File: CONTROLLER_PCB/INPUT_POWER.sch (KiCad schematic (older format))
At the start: 47 parts

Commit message: LED PCB: Changed to 2 layer, added vias and copper (not complete). Controller: Split up ESP32 and input & power sheets in schematic.
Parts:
- added C?: C_Small, symbol C_Small
- added R? (x2): R_Small, symbol R_Small
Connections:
- net GND: now also C?.2, R?.2
- net VIN: now reaches C?.1, C?.1, C?.1, C?.1, C?.1, L?.1, L?.2, R?.1, TP?.1, U?.3 (IN), U?.3 (VIN)
- net at C?.1, C?.1, D?.2 (K)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: now also R?.1
- new net ADC_Vout: C?.1, R?.1, R?.2
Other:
- moved on the sheet: R?, U?A
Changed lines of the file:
@@
 L TS462CDT U?
 U 1 1 5C5A4CCB
-P 6050 6550
-F 0 "U?" H 6050 6750 50  0000 L CNN
-F 1 "TS462CDT" H 6050 6350 50  0000 L CNN
-F 2 "" H 6050 6550 50  0001 C CNN
-F 3 "" H 6050 6550 50  0001 C CNN
-	1    6050 6550
+P 2300 4800
+F 0 "U?" H 2300 5000 50  0000 L CNN
+F 1 "TS462CDT" H 2300 4600 50  0000 L CNN
+F 2 "" H 2300 4800 50  0001 C CNN
+F 3 "" H 2300 4800 50  0001 C CNN
+	1    2300 4800
 	1    0    0    -1
 $EndComp
@@
 L R_Small R?
 U 1 1 5C5A4DE0
-P 10450 1100
-F 0 "R?" V 10650 1050 50  0000 L CNN
-F 1 "R_Small" V 10550 950 50  0000 L CNN
-F 2 "" H 10450 1100 50  0001 C CNN
-F 3 "" H 10450 1100 50  0001 C CNN
-	1    10450 1100
+P 10500 1100
+F 0 "R?" V 10700 1050 50  0000 L CNN
+F 1 "R_Small" V 10600 950 50  0000 L CNN
+F 2 "" H 10500 1100 50  0001 C CNN
+F 3 "" H 10500 1100 50  0001 C CNN
+	1    10500 1100
 	0    -1   -1   0
 $EndComp
@@
 Connection ~ 8200 1700
 Wire Wire Line
-	8950 1100 10350 1100
+	8950 1100 10400 1100
 Wire Wire Line
 	9300 1200 9300 1100
@@
 Wire Wire Line
 	6800 5300 6800 3500
-Wire Wire Line
-	6800 3500 9450 3500
-Wire Wire Line
-	9450 3500 9450 2000
-Wire Wire Line
-	9450 2000 8050 2000
 Wire Wire Line
 	7050 5200 7050 5300
@@
 L GND #PWR?
 U 1 1 5C5A6FF8
-P 5950 7000
-F 0 "#PWR?" H 5950 6750 50  0001 C CNN
-F 1 "GND" H 5950 6850 50  0000 C CNN
-F 2 "" H 5950 7000 50  0001 C CNN
-F 3 "" H 5950 7000 50  0001 C CNN
-	1    5950 7000
+P 2200 5250
+F 0 "#PWR?" H 2200 5000 50  0001 C CNN
+F 1 "GND" H 2200 5100 50  0000 C CNN
+F 2 "" H 2200 5250 50  0001 C CNN
+F 3 "" H 2200 5250 50  0001 C CNN
+	1    2200 5250
 	1    0    0    -1
 $EndComp
@@
 L GND #PWR?
 U 1 1 5C5A7058
-P 5250 6800
-F 0 "#PWR?" H 5250 6550 50  0001 C CNN
-F 1 "GND" H 5250 6650 50  0000 C CNN
-F 2 "" H 5250 6800 50  0001 C CNN
-F 3 "" H 5250 6800 50  0001 C CNN
-	1    5250 6800
-	1    0    0    -1
-$EndComp
-Wire Wire Line
-	6350 6550 6600 6550
-Wire Wire Line
-	6600 6550 6600 7300
-Wire Wire Line
-	6600 7300 5550 7300
-Wire Wire Line
-	5550 7300 5550 6650
-Wire Wire Line
-	5550 6650 5750 6650
-Wire Wire Line
-	5750 6450 5250 6450
-Wire Wire Line
-	5250 6450 5250 6800
-Wire Wire Line
-	5950 6850 5950 7000
+P 1500 5050
+F 0 "#PWR?" H 1500 4800 50  0001 C CNN
+F 1 "GND" H 1500 4900 50  0000 C CNN
+F 2 "" H 1500 5050 50  0001 C CNN
+F 3 "" H 1500 5050 50  0001 C CNN
+	1    1500 5050
+	1    0    0    -1
+$EndComp
+Wire Wire Line
+	2600 4800 2850 4800
+Wire Wire Line
+	2850 4800 2850 5550
+Wire Wire Line
+	2850 5550 1800 5550
+Wire Wire Line
+	1800 5550 1800 4900
+Wire Wire Line
+	1800 4900 2000 4900
+Wire Wire Line
+	2000 4700 1500 4700
+Wire Wire Line
+	1500 4700 1500 5050
+Wire Wire Line
+	2200 5100 2200 5250
 $Comp
 L TEST TP?
@@
 Wire Wire Line
 	5900 3950 5900 3900
+$Comp
+L R_Small R?
+U 1 1 5C58FF67
+P 10300 2000
+F 0 "R?" H 10330 2020 50  0000 L CNN
+F 1 "R_Small" H 10330 1960 50  0000 L CNN
+F 2 "" H 10300 2000 50  0001 C CNN
+F 3 "" H 10300 2000 50  0001 C CNN
+	1    10300 2000
+	1    0    0    -1
+$EndComp
+$Comp
+L GND #PWR?
+U 1 1 5C58FF6D
+P 10300 2250
+F 0 "#PWR?" H 10300 2000 50  0001 C CNN
+F 1 "GND" H 10300 2100 50  0000 C CNN
+F 2 "" H 10300 2250 50  0001 C CNN
+F 3 "" H 10300 2250 50  0001 C CNN
+	1    10300 2250
+	1    0    0    -1
+$EndComp
+$Comp
+L R_Small R?
+U 1 1 5C58FF73
+P 10300 1600
+F 0 "R?" H 10330 1620 50  0000 L CNN
+F 1 "R_Small" H 10330 1560 50  0000 L CNN
+F 2 "" H 10300 1600 50  0001 C CNN
+F 3 "" H 10300 1600 50  0001 C CNN
+	1    10300 1600
+	1    0    0    -1
+$EndComp
+$Comp
+L C_Small C?
+U 1 1 5C58FF79
+P 9800 2000
+F 0 "C?" H 9810 2070 50  0000 L CNN
+F 1 "C_Small" H 9810 1920 50  0000 L CNN
+F 2 "" H 9800 2000 50  0001 C CNN
+F 3 "" H 9800 2000 50  0001 C CNN
+	1    9800 2000
+	1    0    0    -1
+$EndComp
+$Comp
+L GND #PWR?
+U 1 1 5C58FF7F
+P 9800 2250
+F 0 "#PWR?" H 9800 2000 50  0001 C CNN
+F 1 "GND" H 9800 2100 50  0000 C CNN
+F 2 "" H 9800 2250 50  0001 C CNN
+F 3 "" H 9800 2250 50  0001 C CNN
+	1    9800 2250
+	1    0    0    -1
+$EndComp
+Wire Wire Line
+	10300 2250 10300 2100
+Wire Wire Line
+	10300 1900 10300 1700
+Wire Wire Line
+	9800 1900 9800 1800
+Wire Wire Line
+	9600 1800 10300 1800
+Connection ~ 10300 1800
+Wire Wire Line
+	9800 2250 9800 2100
+Text GLabel 9600 1800 0    60   Input ~ 0
+ADC_Vout
+Connection ~ 9800 1800
+Connection ~ 10300 1100
+Wire Wire Line
+	8050 2000 9250 2000
+Wire Wire Line
+	9250 2000 9250 3500
+Wire Wire Line
+	9250 3500 6800 3500
+Wire Wire Line
+	10300 1500 10300 1100
+Text Label 5750 1100 0    60   ~ 0
+VIN
 $EndSCHEMATC

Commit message: Created ESP32 pinout spreadsheet, finished MCU pinout, and added MCU_SUPPORT schematic sheet.
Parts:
- removed C? (x3): C_Small, symbol C_Small
- added C? (x3): 22uF, Capacitors_SMD:C_1206_HandSoldering, symbol C_Small
- C?: value C_Small -> 22uF; footprint (none) -> Capacitors_SMD:C_1206_HandSoldering
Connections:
- net GND: now also C?.2, C?.2, C?.2
- net at D?.1 (A), D?.3 (A), J?.1: now also C?.1
- net at D?.2 (K), L?.1, Q?.3 (S)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: now also C?.1, C?.1
- net ADC_Vout renamed ADC_VOUT
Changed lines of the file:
@@
 $Descr A4 11693 8268
 encoding utf-8
-Sheet 2 3
+Sheet 2 4
 Title ""
 Date ""
@@
 $EndComp
 $Comp
-L C_Small C?
-U 1 1 5C5A4C4F
-P 3500 1300
-F 0 "C?" H 3510 1370 50  0000 L CNN
-F 1 "C_Small" H 3510 1220 50  0000 L CNN
-F 2 "" H 3500 1300 50  0001 C CNN
-F 3 "" H 3500 1300 50  0001 C CNN
-	1    3500 1300
-	1    0    0    -1
-$EndComp
-$Comp
 L L L?
 U 1 1 5C5A4C56
@@
 P 1900 1300
 F 0 "C?" H 1910 1370 50  0000 L CNN
-F 1 "C_Small" H 1910 1220 50  0000 L CNN
-F 2 "" H 1900 1300 50  0001 C CNN
+F 1 "22uF" H 1910 1220 50  0000 L CNN
+F 2 "Capacitors_SMD:C_1206_HandSoldering" H 1900 1300 50  0001 C CNN
 F 3 "" H 1900 1300 50  0001 C CNN
 	1    1900 1300
-	1    0    0    -1
-$EndComp
-$Comp
-L C_Small C?
-U 1 1 5C5A4C79
-P 2000 3350
-F 0 "C?" H 2010 3420 50  0000 L CNN
-F 1 "C_Small" H 2010 3270 50  0000 L CNN
-F 2 "" H 2000 3350 50  0001 C CNN
-F 3 "" H 2000 3350 50  0001 C CNN
-	1    2000 3350
-	1    0    0    -1
-$EndComp
-$Comp
-L C_Small C?
-U 1 1 5C5A4C80
-P 3250 3300
-F 0 "C?" H 3260 3370 50  0000 L CNN
-F 1 "C_Small" H 3260 3220 50  0000 L CNN
-F 2 "" H 3250 3300 50  0001 C CNN
-F 3 "" H 3250 3300 50  0001 C CNN
-	1    3250 3300
 	1    0    0    -1
 $EndComp
@@
 $Comp
 L GND #PWR?
-U 1 1 5C5A4D7A
-P 3500 1550
-F 0 "#PWR?" H 3500 1300 50  0001 C CNN
-F 1 "GND" H 3500 1400 50  0000 C CNN
-F 2 "" H 3500 1550 50  0001 C CNN
-F 3 "" H 3500 1550 50  0001 C CNN
-	1    3500 1550
-	1    0    0    -1
-$EndComp
-$Comp
-L GND #PWR?
 U 1 1 5C5A4D80
 P 4500 1550
@@
 Connection ~ 2650 1550
 Wire Wire Line
-	2850 1100 3950 1100
-Wire Wire Line
 	3000 1250 3000 1100
 Connection ~ 3000 1100
-Wire Wire Line
-	3500 1200 3500 1100
 Connection ~ 3500 1100
-Wire Wire Line
-	3500 1400 3500 1550
 Wire Wire Line
 	4250 1100 7400 1100
@@
 	9800 2250 9800 2100
 Text GLabel 9600 1800 0    60   Input ~ 0
-ADC_Vout
+ADC_VOUT
 Connection ~ 9800 1800
 Connection ~ 10300 1100
@@
 Text Label 5750 1100 0    60   ~ 0
 VIN
+Wire Wire Line
+	2850 1100 3950 1100
+Wire Wire Line
+	3500 1200 3500 1100
+$Comp
+L GND #PWR?
+U 1 1 5C5A4D7A
+P 3500 1550
+F 0 "#PWR?" H 3500 1300 50  0001 C CNN
+F 1 "GND" H 3500 1400 50  0000 C CNN
+F 2 "" H 3500 1550 50  0001 C CNN
+F 3 "" H 3500 1550 50  0001 C CNN
+	1    3500 1550
+	1    0    0    -1
+$EndComp
+Wire Wire Line
+	3500 1400 3500 1550
+$Comp
+L C_Small C?
+U 1 1 5C605751
+P 3500 1300
+F 0 "C?" H 3510 1370 50  0000 L CNN
+F 1 "22uF" H 3510 1220 50  0000 L CNN
+F 2 "Capacitors_SMD:C_1206_HandSoldering" H 3500 1300 50  0001 C CNN
+F 3 "" H 3500 1300 50  0001 C CNN
+	1    3500 1300
+	1    0    0    -1
+$EndComp
+$Comp
+L C_Small C?
+U 1 1 5C605830
+P 2000 3350
+F 0 "C?" H 2010 3420 50  0000 L CNN
+F 1 "22uF" H 2010 3270 50  0000 L CNN
+F 2 "Capacitors_SMD:C_1206_HandSoldering" H 2000 3350 50  0001 C CNN
+F 3 "" H 2000 3350 50  0001 C CNN
+	1    2000 3350
+	1    0    0    -1
+$EndComp
+$Comp
+L C_Small C?
+U 1 1 5C6058EA
+P 3250 3300
+F 0 "C?" H 3260 3370 50  0000 L CNN
+F 1 "22uF" H 3260 3220 50  0000 L CNN
+F 2 "Capacitors_SMD:C_1206_HandSoldering" H 3250 3300 50  0001 C CNN
+F 3 "" H 3250 3300 50  0001 C CNN
+	1    3250 3300
+	1    0    0    -1
+$EndComp
 $EndSCHEMATC

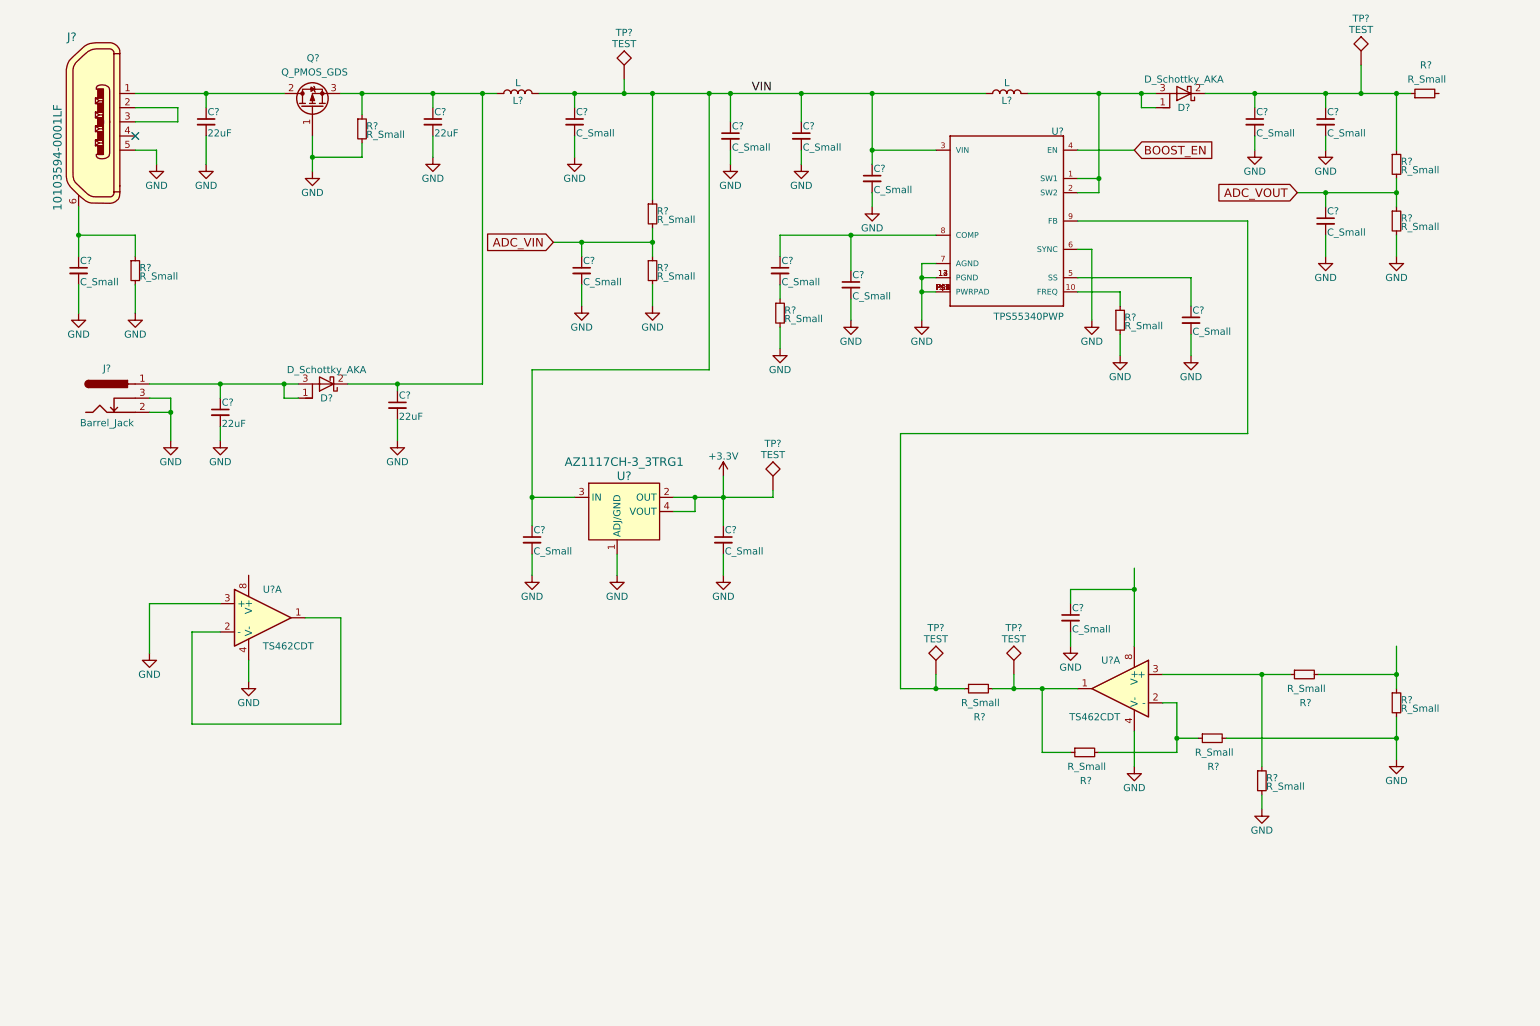
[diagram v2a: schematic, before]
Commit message: Added input filtering, and assigned footprints to most components, several remain.
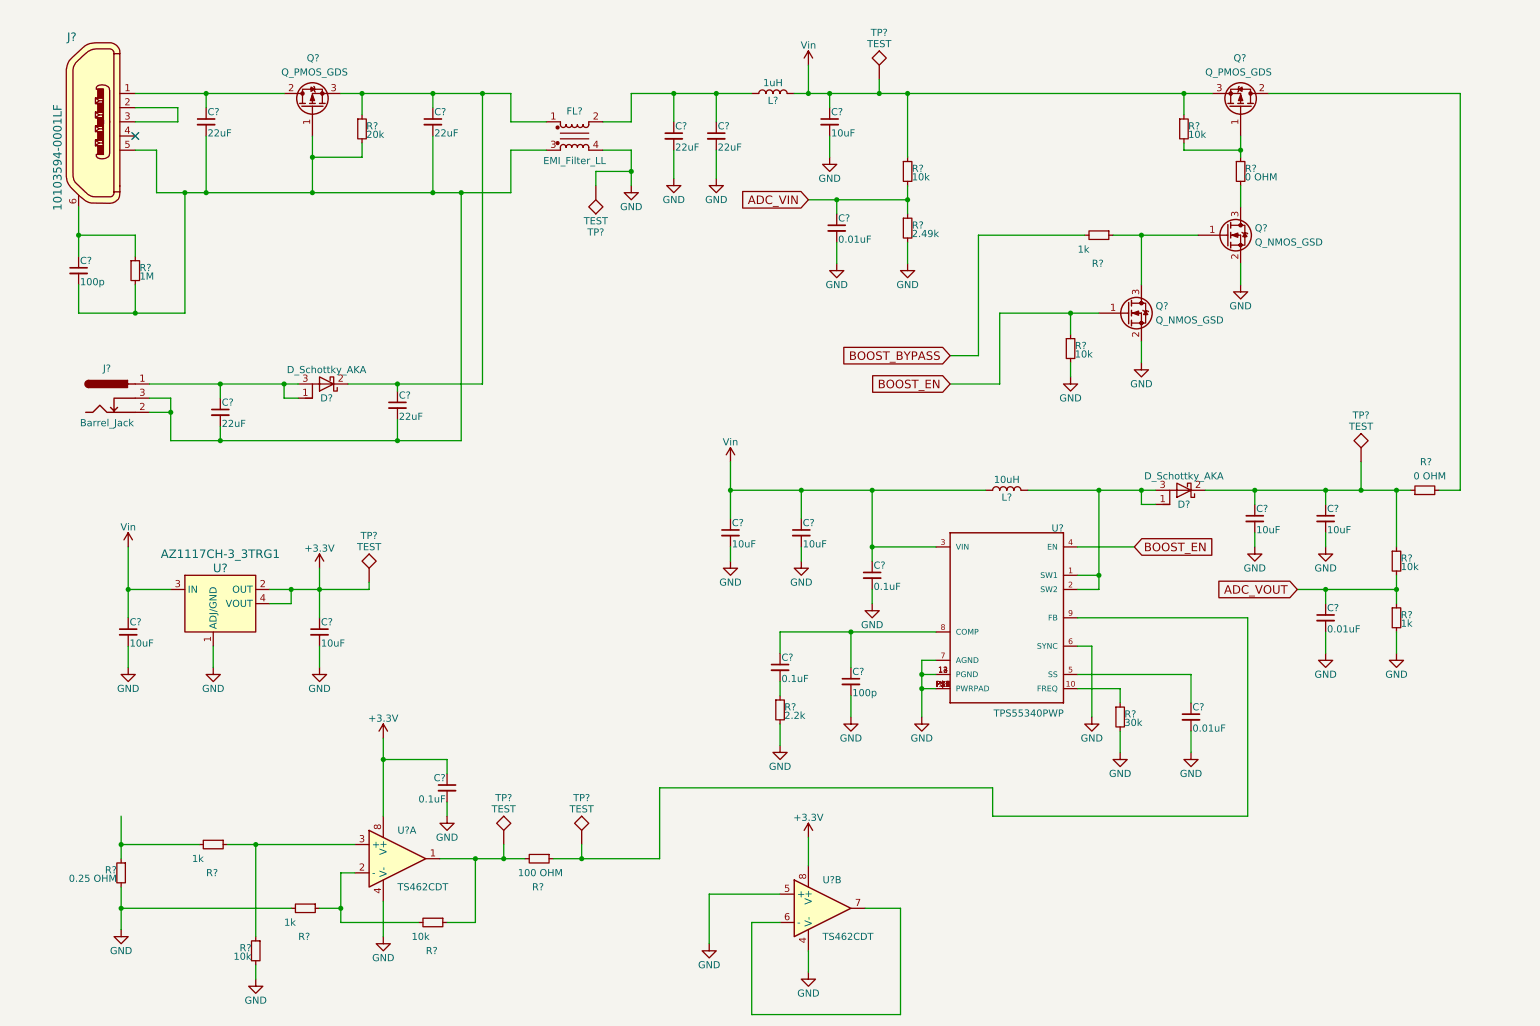
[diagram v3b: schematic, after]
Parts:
- removed C? (x10): C_Small, symbol C_Small
- removed U?: TS462CDT, symbol TS462CDT
- added C? (x5): 10uF, Capacitors_SMD:C_0805_HandSoldering, symbol C_Small
- added C? (x2): 0.01uF, Capacitors_SMD:C_0603_HandSoldering, symbol C_Small
- added C? (x2): 0.1uF, Capacitors_SMD:C_0603_HandSoldering, symbol C_Small
- added C?: 100p, Capacitors_SMD:C_0603_HandSoldering, symbol C_Small
- added C? (x2): 22uF, Capacitors_SMD:C_1206_HandSoldering, symbol C_Small
- added FL?: EMI_Filter_LL, CustomFootprints:IND_ACM12V-701-2PL-TL00_FixedPadNumbers, symbol EMI_Filter_LL
- added Q?: Q_PMOS_GDS, TO_SOT_Packages_SMD:TO-252-2_Rectifier, symbol Q_PMOS_GDS
- added Q? (x2): Q_NMOS_GSD, TO_SOT_Packages_SMD:SOT-23, symbol Q_NMOS_GSD
- added R?: 0 OHM, Resistors_SMD:R_0603_HandSoldering, symbol R_Small
- added R? (x2): 10k, Resistors_SMD:R_0603_HandSoldering, symbol R_Small
- added R?: 1k, Resistors_SMD:R_0603_HandSoldering, symbol R_Small
- added TP?: TEST, Measurement_Points:Measurement_Point_Round-SMD-Pad_Small, symbol TEST
- added U?: TS462CDT, digikey-footprints:SOIC-8_W3.9mm, symbol TS462CDT
- C?: value C_Small -> 0.01uF; footprint (none) -> Capacitors_SMD:C_0603_HandSoldering
- C? (x2): value C_Small -> 10uF; footprint (none) -> Capacitors_SMD:C_0805_HandSoldering
- C?: value C_Small -> 0.1uF; footprint (none) -> Capacitors_SMD:C_0603_HandSoldering
- C?: value C_Small -> 100p; footprint (none) -> Capacitors_SMD:C_0603_HandSoldering
- D? (x2): footprint (none) -> PowerDI5:Diodes_Incorporated_POWERDI_5
- J?: footprint (none) -> Connectors:BARREL_JACK
- J?: footprint (none) -> Connectors:USB_Micro-B_10103594-0001LF
- L?: value L -> 1uH; footprint (none) -> CustomFootprints:L_12x12mm_h8mm_hand_soldering; P/N (none) -> SRR1260-1R0Y
- L?: value L -> 10uH; footprint (none) -> CustomFootprints:L_12x12mm_h8mm_hand_soldering; P/N (none) -> SRR1280-100M
- Q?: footprint (none) -> TO_SOT_Packages_SMD:TO-252-2_Rectifier
- R? (x3): value R_Small -> 1k; footprint (none) -> Resistors_SMD:R_0603_HandSoldering
- R? (x4): value R_Small -> 10k; footprint (none) -> Resistors_SMD:R_0603_HandSoldering
- R?: value R_Small -> 30k; footprint (none) -> Resistors_SMD:R_0603_HandSoldering
- R?: value R_Small -> 2.2k; footprint (none) -> Resistors_SMD:R_0603_HandSoldering
- R?: value R_Small -> 0.25 OHM; footprint (none) -> Resistors_SMD:R_1206_HandSoldering; P/N (none) -> PT1206FR-070R25L
- R?: value R_Small -> 100 OHM; footprint (none) -> Resistors_SMD:R_0603_HandSoldering
- R?: value R_Small -> 2.49k; footprint (none) -> Resistors_SMD:R_0603_HandSoldering
- R?: value R_Small -> 20k; footprint (none) -> Resistors_SMD:R_0603_HandSoldering
- R?: value R_Small -> 0 OHM; footprint (none) -> Resistors_SMD:R_0603_HandSoldering
- R?: value R_Small -> 1M; footprint (none) -> Resistors_SMD:R_0603_HandSoldering
- TP? (x4): footprint (none) -> Measurement_Points:Measurement_Point_Round-SMD-Pad_Small
- U?: footprint (none) -> digikey-footprints:SOIC-8_W3.9mm
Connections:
- net +3V3: now also U?.8 (V+), C?.1, C?.1, U?.8 (V+)
- net ADC_VIN: now also C?.1
- net BOOST_EN: now also Q?.1 (G), R?.1
- net GND: now also C?.2, C?.2, C?.2, C?.2, C?.2, C?.2, C?.2, C?.2, C?.2, C?.2, C?.2, FL?.4, Q?.2 (S), Q?.2 (S), R?.2, TP?.1, U?.4 (V-), U?.5 (+); no longer C?.2, C?.2, C?.2, C?.2, C?.2, J?.2, J?.3, J?.5, Q?.1 (G), R?.2, R?.2
- net at D?.2 (K), R?.1, R?.1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: now also C?.1, C?.1
- net at C?.1, C?.1, D?.2 (K)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: now also FL?.1; no longer L?.1
- net at U?.5 (SS): now also C?.1
- net at U?.8 (COMP): now also C?.1, C?.1
- net at R?.1: now also C?.2
- net at R?.2: now also Q?.2 (D)
- net VIN renamed Vin
- net Vin: now also C?.1, C?.1, Q?.3 (S), R?.1
- new net: C?.2, C?.2, C?.2, C?.2, C?.2, FL?.3, J?.2, J?.3, J?.5, Q?.1 (G), R?.2, R?.2
- new net: C?.1, C?.1, FL?.2, L?.1
- new net: U?.6 (-), U?.7
- new net: Q?.1 (G), R?.1, R?.2
- new net: Q?.3 (D), R?.2
- new net: Q?.1 (G), Q?.3 (D), R?.1
- new net BOOST_BYPASS: R?.2
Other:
- moved on the sheet: C?, D?, L?, R?, TP?, U?, U?A
